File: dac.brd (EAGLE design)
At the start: 77.5 x 54.3 mm, 69 parts, among them IC1 TLC7733PW, IC2 TC1262-3.3VDB, IC3 LP3879, IC4 XHRA-2HPA, IC5 RCLAMP0502ASMD, IC6 PCM1794, Q1_24 ASF/V_KSC3225KSC, Q2_24M576 ASF/V_KSC3225KSC, Q3_22M5792 ASF/V_KSC3225KSC, U1 OPA1644AIPW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

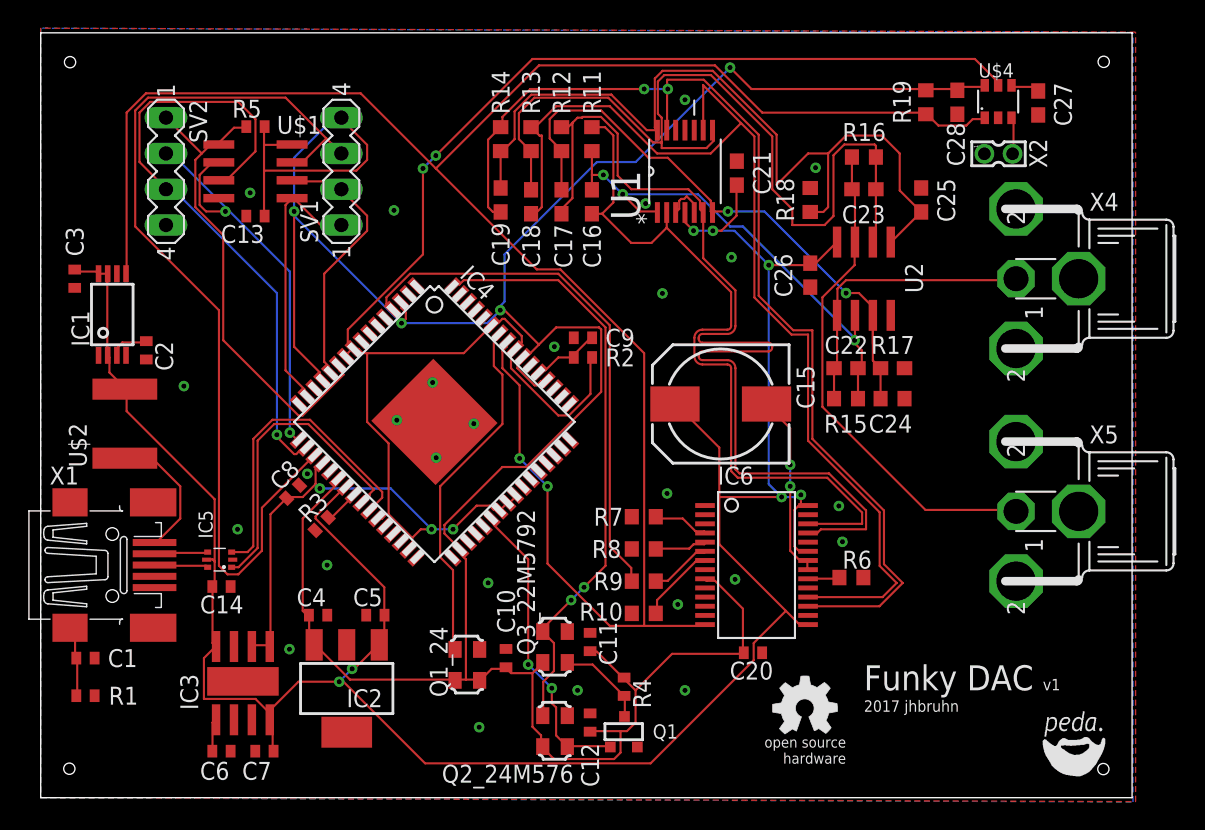
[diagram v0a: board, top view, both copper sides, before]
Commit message: Fix wrong XHRA-2HPA package size
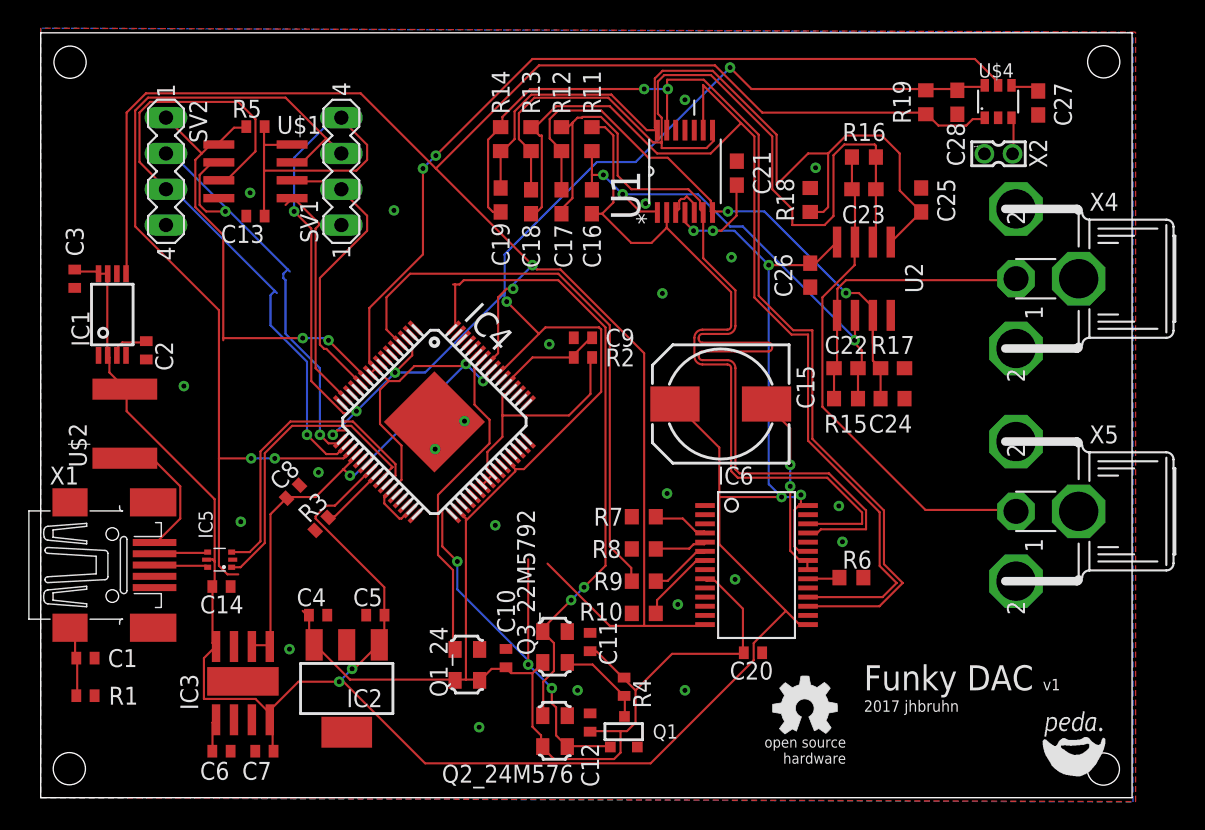
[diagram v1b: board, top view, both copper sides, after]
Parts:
- IC4: value XHRA-2HPA -> XHRA-2HPAREAL; device jean:TQFP64 -> jean:TQFP64-10X10
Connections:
- net +1V: now also IC4.52
- net +3V3: no longer IC4.52
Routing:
- net CLK_SEL: track 21.5 -> 34.6 mm, vias 2 -> 3
- net !RESET: track 150.1 -> 141.3 mm
- net +3V3: track 222.4 -> 218.2 mm, vias 4 -> 6
- net MCLK: track 42.6 -> 45.6 mm
- net +1V: track 138.9 -> 136.0 mm
- net BCLK: track 37.9 -> 40.5 mm
- net N$6: track 4.93 -> 7.46 mm
- net SPI_IO1: track 30.6 -> 33.1 mm
- net +5V: track 175.4 -> 177.6 mm
- net N$7: track 2.47 -> 4.57 mm
- net SPI_CLK: track 18.9 -> 20.9 mm
- net SPI_IO2: track 44.9 -> 46.9 mm
- net 24MHZ_CLK: track 25.2 -> 23.4 mm
- net SPI_CS: track 34.7 -> 33.1 mm, vias 0 -> 2
- net SPI_IO3: track 66.8 -> 65.7 mm, vias 0 -> 2
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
